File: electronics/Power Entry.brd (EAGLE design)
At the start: 101.6 x 101.6 mm, 13 parts, among them J1 1-770967-0, J2 1-770969-0, K1 ALQ3F12, P1 703W-00/04

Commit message: Update Power Entry.brd
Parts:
- moved C2 88.1 mm to (80.0, 19.1), turned to 270 degrees
- moved R4 39.2 mm to (29.2, 62.2), turned to 270 degrees
- moved R3 35.9 mm to (22.9, 57.1), turned to 0 degrees
- moved C1 31.2 mm to (80.0, 55.9), turned to 270 degrees
- moved R2 28.5 mm to (22.9, 49.5)
- moved P1 25.4 mm to (54.6, 11.4), flipped to the top
- moved R1 23.4 mm to (33.0, 40.6)
- moved D1 18.9 mm to (21.6, 44.5), turned to 90 degrees
- moved BR1 13.5 mm to (52.1, 41.9)
- moved C3 13.1 mm to (19.1, 34.3), turned to 0 degrees
- moved K1 6.84 mm to (26.7, 26.7)
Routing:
- net N$3: track 0.00 -> 94.4 mm
- net +170V: track 0.00 -> 83.2 mm
- net N$2: track 0.00 -> 57.6 mm
- net N$6: track 0.00 -> 43.2 mm
- net N$8: track 0.00 -> 26.4 mm
- net N$1: track 0.00 -> 20.0 mm
- net N$4: track 0.00 -> 16.8 mm
- added copper zone on layer 1, net GND
- added copper zone on layer 16, net GND
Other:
- board size 101.6 x 101.6 mm -> 99.1 x 74.9 mm

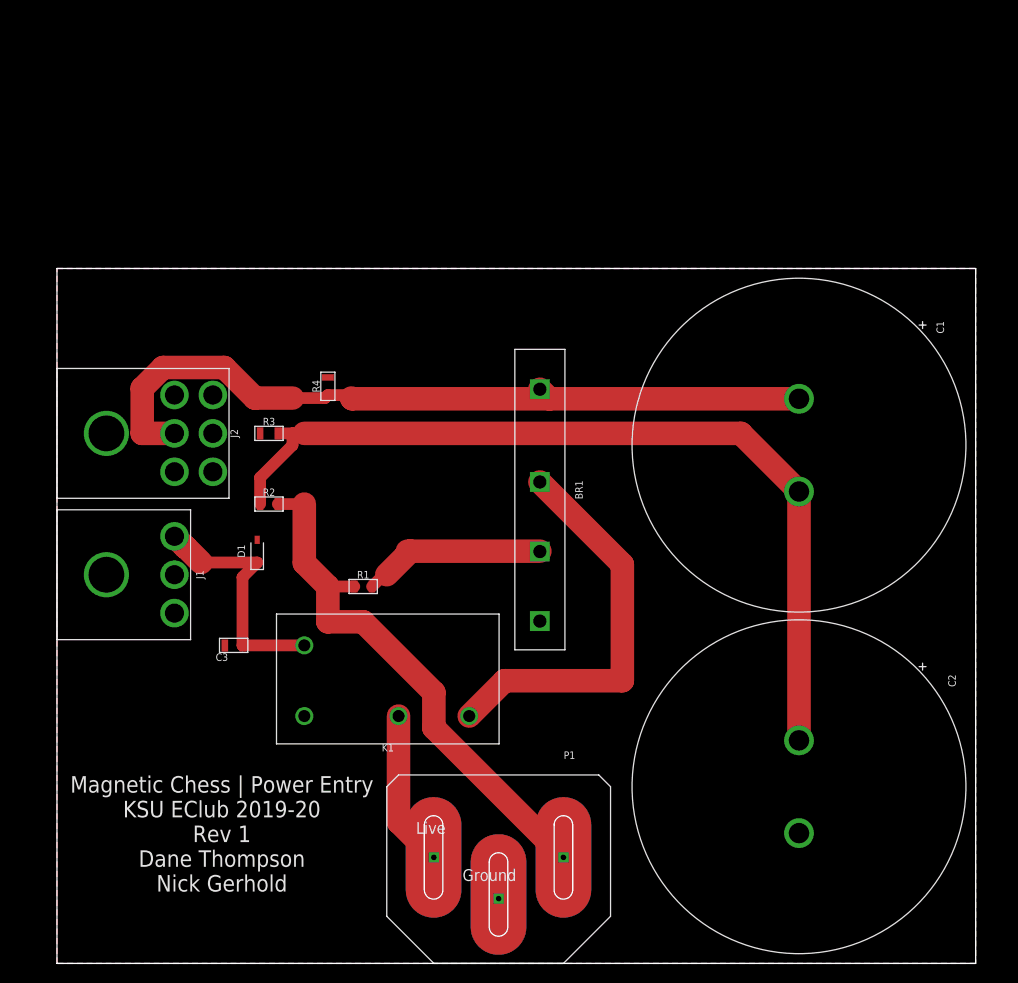
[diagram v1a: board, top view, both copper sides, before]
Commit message: Added mounting holes
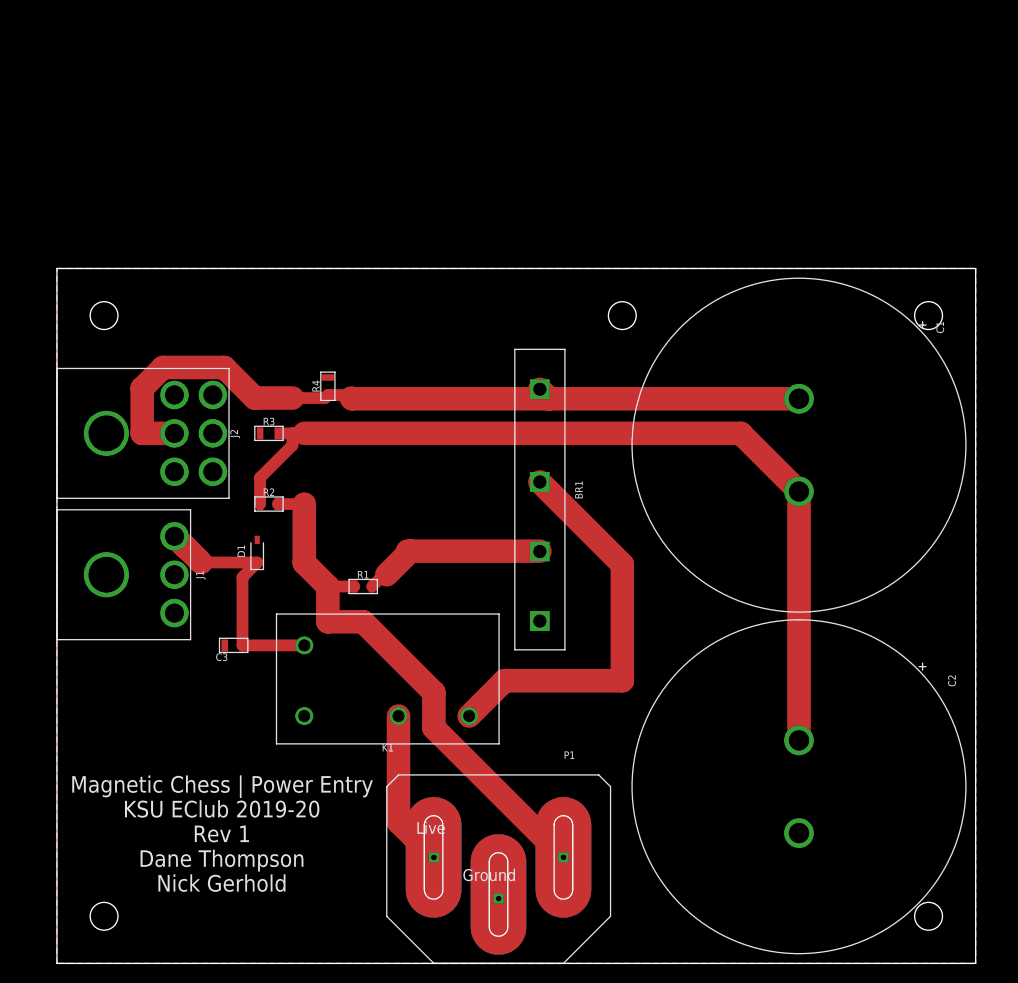
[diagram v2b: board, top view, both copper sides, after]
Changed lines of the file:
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@@
 <layers>
 <layer number="1" name="Top" color="4" fill="1" visible="yes" active="yes"/>
+<layer number="2" name="Route2" color="16" fill="1" visible="no" active="no"/>
+<layer number="3" name="Route3" color="17" fill="1" visible="no" active="no"/>
+<layer number="4" name="Route4" color="18" fill="1" visible="no" active="no"/>
+<layer number="5" name="Route5" color="19" fill="1" visible="no" active="no"/>
+<layer number="6" name="Route6" color="25" fill="1" visible="no" active="no"/>
+<layer number="7" name="Route7" color="26" fill="1" visible="no" active="no"/>
+<layer number="8" name="Route8" color="27" fill="1" visible="no" active="no"/>
+<layer number="9" name="Route9" color="28" fill="1" visible="no" active="no"/>
+<layer number="10" name="Route10" color="29" fill="1" visible="no" active="no"/>
+<layer number="11" name="Route11" color="30" fill="1" visible="no" active="no"/>
+<layer number="12" name="Route12" color="20" fill="1" visible="no" active="no"/>
+<layer number="13" name="Route13" color="21" fill="1" visible="no" active="no"/>
+<layer number="14" name="Route14" color="22" fill="1" visible="no" active="no"/>
+<layer number="15" name="Route15" color="23" fill="1" visible="no" active="no"/>
 <layer number="16" name="Bottom" color="1" fill="1" visible="yes" active="yes"/>
 <layer number="17" name="Pads" color="2" fill="1" visible="yes" active="yes"/>
@@
 <layer number="27" name="tValues" color="7" fill="1" visible="yes" active="yes"/>
 <layer number="28" name="bValues" color="7" fill="1" visible="yes" active="yes"/>
-<layer number="29" name="tStop" color="7" fill="3" visible="no" active="yes"/>
-<layer number="30" name="bStop" color="7" fill="6" visible="no" active="yes"/>
+<layer number="29" name="tStop" color="7" fill="3" visible="yes" active="yes"/>
+<layer number="30" name="bStop" color="7" fill="6" visible="yes" active="yes"/>
 <layer number="31" name="tCream" color="7" fill="4" visible="no" active="yes"/>
 <layer number="32" name="bCream" color="7" fill="5" visible="no" active="yes"/>
@@
 <layer number="43" name="vRestrict" color="2" fill="10" visible="yes" active="yes"/>
 <layer number="44" name="Drills" color="7" fill="1" visible="no" active="yes"/>
-<layer number="45" name="Holes" color="7" fill="1" visible="no" active="yes"/>
+<layer number="45" name="Holes" color="7" fill="1" visible="yes" active="yes"/>
 <layer number="46" name="Milling" color="3" fill="1" visible="no" active="yes"/>
 <layer number="47" name="Measures" color="7" fill="1" visible="no" active="yes"/>
 <layer number="48" name="Document" color="7" fill="1" visible="yes" active="yes"/>
 <layer number="49" name="Reference" color="7" fill="1" visible="yes" active="yes"/>
+<layer number="50" name="dxf" color="7" fill="1" visible="no" active="no"/>
 <layer number="51" name="tDocu" color="7" fill="1" visible="yes" active="yes"/>
 <layer number="52" name="bDocu" color="7" fill="1" visible="yes" active="yes"/>
@@
 <layer number="97" name="Info" color="7" fill="1" visible="no" active="no"/>
 <layer number="98" name="Guide" color="6" fill="1" visible="no" active="no"/>
+<layer number="99" name="SpiceOrder" color="5" fill="1" visible="no" active="no"/>
+<layer number="200" name="200bmp" color="7" fill="1" visible="yes" active="yes"/>
+<layer number="250" name="Descript" color="7" fill="1" visible="yes" active="yes"/>
+<layer number="251" name="SMDround" color="7" fill="1" visible="yes" active="yes"/>
 </layers>
 <board>
@@
 Dane Thompson
 Nick Gerhold</text>
+<circle x="5.08" y="5.08" radius="4.016090625" width="0" layer="41"/>
+<circle x="5.08" y="5.08" radius="4.016090625" width="0" layer="42"/>
+<circle x="5.08" y="5.08" radius="4.016090625" width="0" layer="29"/>
+<circle x="5.08" y="5.08" radius="4.016090625" width="0" layer="30"/>
+<hole x="5.08" y="5.08" drill="3"/>
+<circle x="93.98" y="5.08" radius="4.016090625" width="0" layer="41"/>
+<circle x="93.98" y="5.08" radius="4.016090625" width="0" layer="42"/>
+<circle x="93.98" y="5.08" radius="4.016090625" width="0" layer="29"/>
+<circle x="93.98" y="5.08" radius="4.016090625" width="0" layer="30"/>
+<hole x="93.98" y="5.08" drill="3"/>
+<circle x="93.98" y="69.85" radius="4.016090625" width="0" layer="41"/>
+<circle x="93.98" y="69.85" radius="4.016090625" width="0" layer="42"/>
+<circle x="93.98" y="69.85" radius="4.016090625" width="0" layer="29"/>
+<circle x="93.98" y="69.85" radius="4.016090625" width="0" layer="30"/>
+<hole x="93.98" y="69.85" drill="3"/>
+<circle x="5.08" y="69.85" radius="4.016090625" width="0" layer="41"/>
+<circle x="5.08" y="69.85" radius="4.016090625" width="0" layer="42"/>
+<circle x="5.08" y="69.85" radius="4.016090625" width="0" layer="29"/>
+<circle x="5.08" y="69.85" radius="4.016090625" width="0" layer="30"/>
+<hole x="5.08" y="69.85" drill="3"/>
+<circle x="60.96" y="69.85" radius="4.016090625" width="0" layer="41"/>
+<circle x="60.96" y="69.85" radius="4.016090625" width="0" layer="42"/>
+<circle x="60.96" y="69.85" radius="4.016090625" width="0" layer="29"/>
+<circle x="60.96" y="69.85" radius="4.016090625" width="0" layer="30"/>
+<hole x="60.96" y="69.85" drill="3"/>
 </plain>
 <attributes>
